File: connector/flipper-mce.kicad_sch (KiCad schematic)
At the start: 69 parts, among them J3 USB_C_Receptacle_USB2.0, SW1 USER1, SW2 USER2, SW3 USER, U2 XC6206P332MR, U3 RP2040, U4 LY68L6400SLIT, U5 W25Q16JVUXIQ, Y1 12 Mhz

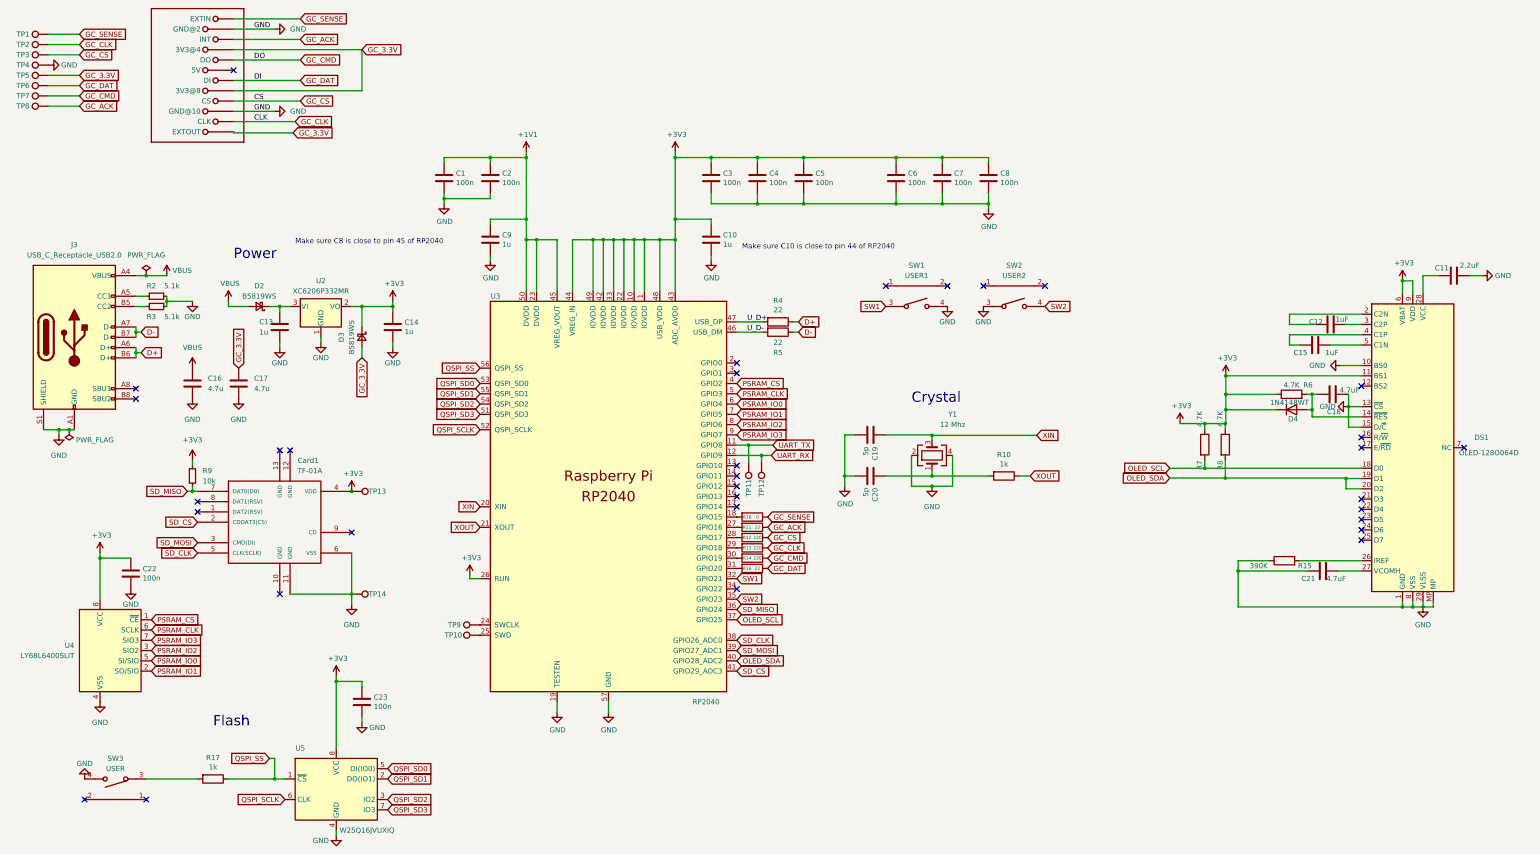
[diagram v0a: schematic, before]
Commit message: Fix Cap values
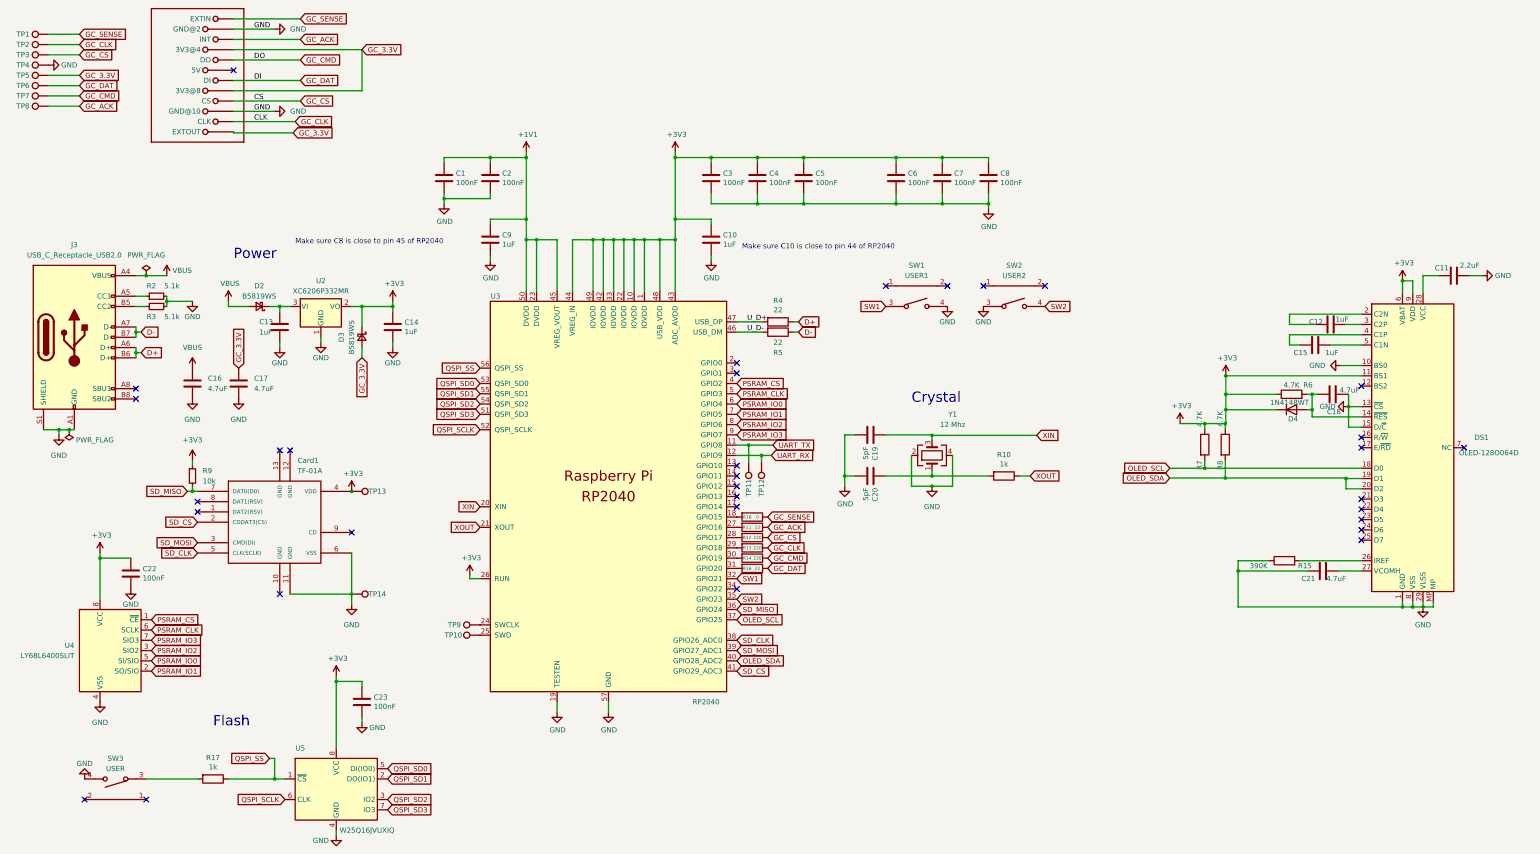
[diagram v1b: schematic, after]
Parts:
- C1, C2, C22, C23, C3, C4, C5, C6, C7, C8: value 100n -> 100nF
- C10, C13, C14, C9: value 1u -> 1uF
- C16, C17: value 4.7u -> 4.7uF
- C19, C20: value 5p -> 5pF
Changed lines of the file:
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@@
 			)
 		)
-		(property "Value" "100n"
+		(property "Value" "100nF"
 			(at 277.241 79.883 0)
 			(effects
@@
 			)
 		)
-		(property "Value" "100n"
+		(property "Value" "100nF"
 			(at 122.301 209.423 0)
 			(effects
@@
 			)
 		)
-		(property "Value" "100n"
+		(property "Value" "100nF"
 			(at 231.521 79.883 0)
 			(effects
@@
 			)
 		)
-		(property "Value" "100n"
+		(property "Value" "100nF"
 			(at 254.381 79.883 0)
 			(effects
@@
 			)
 		)
-		(property "Value" "100n"
+		(property "Value" "100nF"
 			(at 265.811 79.883 0)
 			(effects
@@
 			)
 		)
-		(property "Value" "100n"
+		(property "Value" "100nF"
 			(at 154.051 79.883 0)
 			(effects
@@
 			)
 		)
-		(property "Value" "4.7u"
+		(property "Value" "4.7uF"
 			(at 81.28 130.8099 0)
 			(effects
@@
 			)
 		)
-		(property "Value" "5p"
+		(property "Value" "5pF"
 			(at 243.967 145.161 0)
 			(effects
@@
 			)
 		)
-		(property "Value" "1u"
+		(property "Value" "1uF"
 			(at 154.051 95.123 0)
 			(effects
@@
 			)
 		)
-		(property "Value" "1u"
+		(property "Value" "1uF"
 			(at 93.98 116.84 0)
 			(effects
@@
 			)
 		)
-		(property "Value" "1u"
+		(property "Value" "1uF"
 			(at 208.661 95.123 0)
 			(effects
@@
 			)
 		)
-		(property "Value" "100n"
+		(property "Value" "100nF"
 			(at 208.661 79.883 0)
 			(effects
@@
 			)
 		)
-		(property "Value" "5p"
+		(property "Value" "5pF"
 			(at 243.967 155.321 0)
 			(effects
@@
 			)
 		)
-		(property "Value" "100n"
+		(property "Value" "100nF"
 			(at 220.091 79.883 0)
 			(effects
@@
 			)
 		)
-		(property "Value" "100n"
+		(property "Value" "100nF"
 			(at 65.151 177.673 0)
 			(effects
@@
 			)
 		)
-		(property "Value" "4.7u"
+		(property "Value" "4.7uF"
 			(at 92.71 130.8099 0)
 			(effects
@@
 			)
 		)
-		(property "Value" "1u"
+		(property "Value" "1uF"
 			(at 129.921 116.713 0)
 			(effects
@@
 			)
 		)
-		(property "Value" "100n"
+		(property "Value" "100nF"
 			(at 142.621 79.883 0)
 			(effects
